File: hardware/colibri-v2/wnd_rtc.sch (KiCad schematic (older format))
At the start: 7 parts

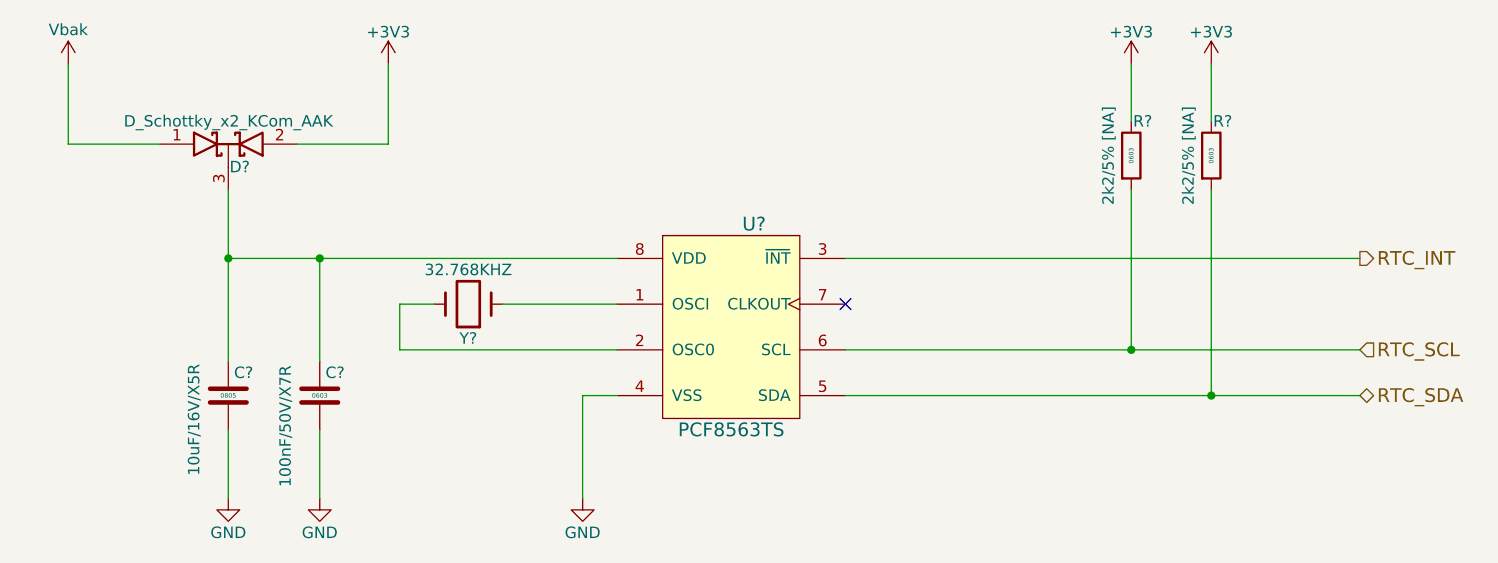
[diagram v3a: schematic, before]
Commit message: Added ext_sensors.sch sheet
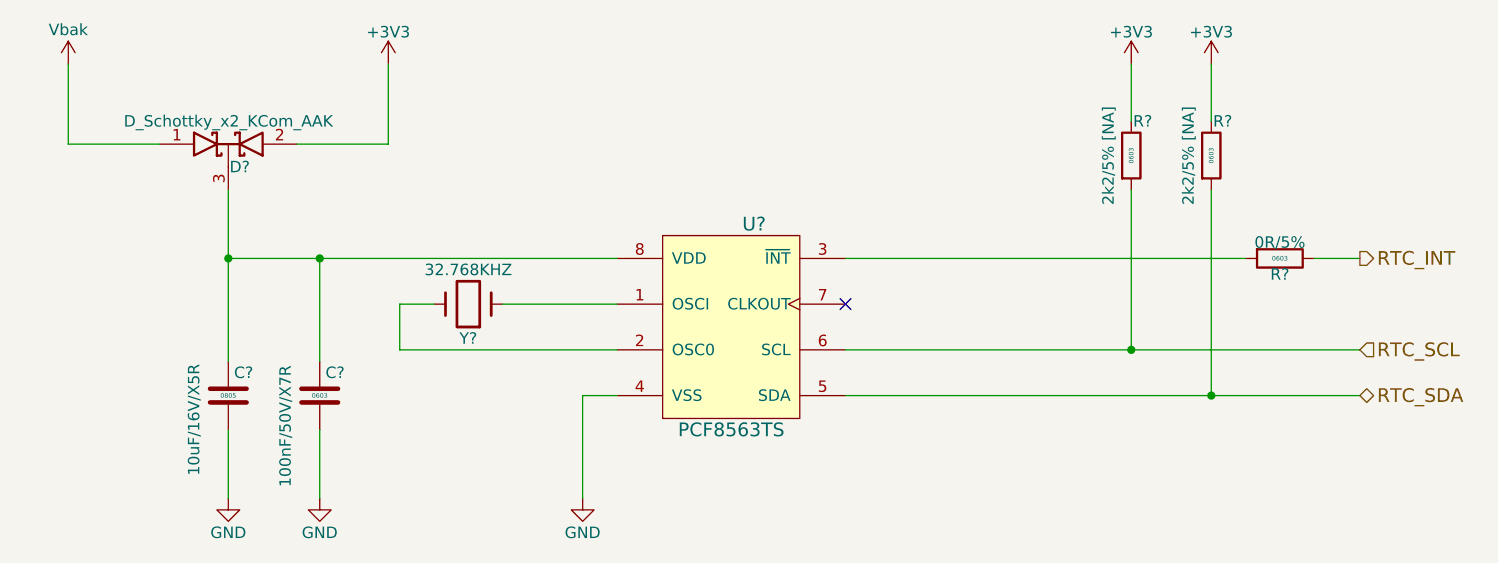
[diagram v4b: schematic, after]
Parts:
- added R?: 0R/5%, Resistors_SMD:R_0603, symbol R_SMT
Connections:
- net RTC_INT: now also R?.1; no longer U?.3 (~INT)
- new net: R?.2, U?.3 (~INT)
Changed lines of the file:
@@
 $Descr A4 11693 8268
 encoding utf-8
-Sheet 19 28
+Sheet 18 28
 Title ""
 Date ""
@@
 NoConn ~ 6000 3300
 Wire Wire Line
-	6000 3100 8250 3100
-Wire Wire Line
 	6000 3500 8250 3500
 Wire Wire Line
@@
 	7600 2800 7600 3700
 Connection ~ 7600 3700
+$Comp
+L R_SMT R?
+U 1 1 56CA065D
+P 7900 3100
+F 0 "R?" V 7970 3100 50  0000 C CNN
+F 1 "0R/5%" V 7830 3100 50  0000 C CNN
+F 2 "Resistors_SMD:R_0603" V 8050 3100 30  0001 C CNN
+F 3 "" V 7980 3100 30  0000 C CNN
+F 4 "0603" V 7900 3100 20  0000 C CNN "SMT"
+F 5 "1469739" V 8100 3100 30  0001 C CNN "Part"
+F 6 "Farnell" V 8150 3100 30  0001 C CNN "Provider"
+	1    7900 3100
+	0    1    1    0
+$EndComp
+Wire Wire Line
+	6000 3100 7750 3100
+Wire Wire Line
+	8050 3100 8250 3100
 $EndSCHEMATC

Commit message: Resolving ERC problems
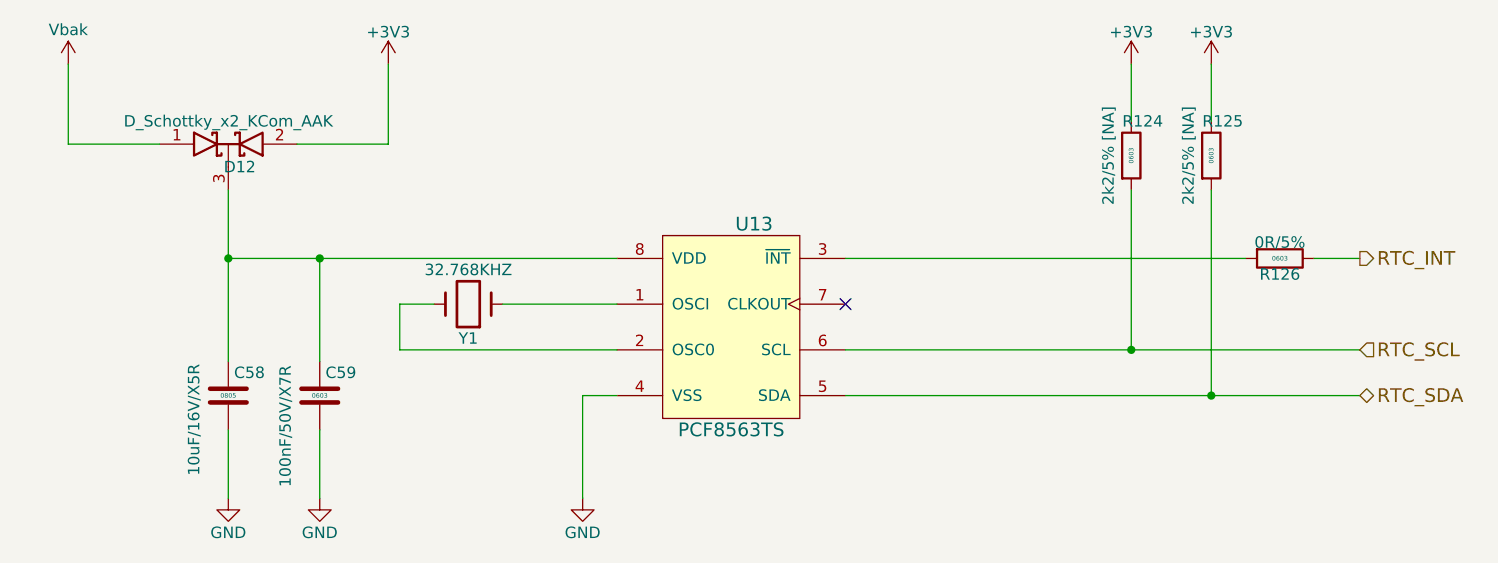
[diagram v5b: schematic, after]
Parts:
- gave numbers to parts that had none: 8
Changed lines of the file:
@@
 EESchema Schematic File Version 2
+LIBS:colibri-wnd-rescue
 LIBS:power
 LIBS:device
@@
 $EndDescr
 $Comp
-L PCF8563TS U?
+L PCF8563TS U13
 U 1 1 565FD554
 P 5500 3400
-F 0 "U?" H 5600 3850 60  0000 C CNN
+F 0 "U13" H 5600 3850 60  0000 C CNN
 F 1 "PCF8563TS" H 5500 2950 60  0000 C CNN
 F 2 "Housings_SSOP:TSSOP-8_3x3mm_Pitch0.65mm" H 5500 2850 60  0001 C CNN
@@
 $EndComp
 $Comp
-L GND #PWR?
+L GND #PWR0161
 U 1 1 565FD5E2
 P 4850 4150
-F 0 "#PWR?" H 4850 3900 50  0001 C CNN
+F 0 "#PWR0161" H 4850 3900 50  0001 C CNN
 F 1 "GND" H 4850 4000 50  0000 C CNN
 F 2 "" H 4850 4150 50  0000 C CNN
@@
 $EndComp
 $Comp
-L +3V3 #PWR?
+L +3V3 #PWR0162
 U 1 1 565FD5F8
 P 4000 2250
-F 0 "#PWR?" H 4000 2100 50  0001 C CNN
+F 0 "#PWR0162" H 4000 2100 50  0001 C CNN
 F 1 "+3V3" H 4000 2390 50  0000 C CNN
 F 2 "" H 4000 2250 50  0000 C CNN
@@
 $EndComp
 $Comp
-L Crystal Y?
+L Crystal Y1
 U 1 1 565FE8B8
 P 4350 3300
-F 0 "Y?" H 4350 3450 50  0000 C CNN
+F 0 "Y1" H 4350 3450 50  0000 C CNN
 F 1 "32.768KHZ" H 4350 3150 50  0000 C CNN
 F 2 "" H 4350 3300 60  0001 C CNN
@@
 	4850 3700 4850 4150
 $Comp
-L D_Schottky_x2_KCom_AAK D?
+L D_Schottky_x2_KCom_AAK D12
 U 1 1 565FE933
 P 3300 2600
-F 0 "D?" H 3350 2500 50  0000 C CNN
+F 0 "D12" H 3350 2500 50  0000 C CNN
 F 1 "D_Schottky_x2_KCom_AAK" H 3300 2700 50  0000 C CNN
 F 2 "" H 3300 2600 50  0000 C CNN
@@
 	2600 2600 3000 2600
 $Comp
-L C_SMT C?
+L C_SMT C59
 U 1 1 56601B22
 P 3700 3700
-F 0 "C?" H 3725 3800 50  0000 L CNN
+F 0 "C59" H 3725 3800 50  0000 L CNN
 F 1 "100nF/50V/X7R" V 3550 3300 50  0000 L CNN
 F 2 "Capacitors_SMD:C_0603" H 3730 3550 30  0001 L CNN
@@
 $EndComp
 $Comp
-L C_SMT C?
+L C_SMT C58
 U 1 1 56601B2C
 P 3300 3700
-F 0 "C?" H 3325 3800 50  0000 L CNN
+F 0 "C58" H 3325 3800 50  0000 L CNN
 F 1 "10uF/16V/X5R" V 3150 3350 50  0000 L CNN
 F 2 "Capacitors_SMD:C_0603" H 3330 3550 30  0001 L CNN
@@
 $EndComp
 $Comp
-L GND #PWR?
+L GND #PWR0163
 U 1 1 56601B52
 P 3700 4150
-F 0 "#PWR?" H 3700 3900 50  0001 C CNN
+F 0 "#PWR0163" H 3700 3900 50  0001 C CNN
 F 1 "GND" H 3700 4000 50  0000 C CNN
 F 2 "" H 3700 4150 50  0000 C CNN
@@
 $EndComp
 $Comp
-L GND #PWR?
+L GND #PWR0164
 U 1 1 56601B71
 P 3300 4150
-F 0 "#PWR?" H 3300 3900 50  0001 C CNN
+F 0 "#PWR0164" H 3300 3900 50  0001 C CNN
 F 1 "GND" H 3300 4000 50  0000 C CNN
 F 2 "" H 3300 4150 50  0000 C CNN
@@
 Connection ~ 3300 3100
 $Comp
-L Vbak #PWR?
+L Vbak #PWR0165
 U 1 1 56602BA4
 P 2600 2250
-F 0 "#PWR?" H 2600 2100 50  0001 C CNN
+F 0 "#PWR0165" H 2600 2100 50  0001 C CNN
 F 1 "Vbak" H 2600 2400 50  0000 C CNN
 F 2 "" H 2600 2250 50  0000 C CNN
@@
 	6000 3700 8250 3700
 $Comp
-L +3V3 #PWR?
+L +3V3 #PWR0166
 U 1 1 56603479
 P 7250 2250
-F 0 "#PWR?" H 7250 2100 50  0001 C CNN
+F 0 "#PWR0166" H 7250 2100 50  0001 C CNN
 F 1 "+3V3" H 7250 2390 50  0000 C CNN
 F 2 "" H 7250 2250 50  0000 C CNN
@@
 $EndComp
 $Comp
-L +3V3 #PWR?
+L +3V3 #PWR0167
 U 1 1 566034CA
 P 7600 2250
-F 0 "#PWR?" H 7600 2100 50  0001 C CNN
+F 0 "#PWR0167" H 7600 2100 50  0001 C CNN
 F 1 "+3V3" H 7600 2390 50  0000 C CNN
 F 2 "" H 7600 2250 50  0000 C CNN
@@
 $EndComp
 $Comp
-L R_SMT R?
+L R_SMT R125
 U 1 1 56606072
 P 7600 2650
-F 0 "R?" H 7650 2800 50  0000 C CNN
+F 0 "R125" H 7650 2800 50  0000 C CNN
 F 1 "2k2/5% [NA]" V 7500 2650 50  0000 C CNN
 F 2 "Resistors_SMD:R_0603" V 7750 2650 30  0001 C CNN
@@
 $EndComp
 $Comp
-L R_SMT R?
+L R_SMT R124
 U 1 1 5660607C
 P 7250 2650
-F 0 "R?" H 7300 2800 50  0000 C CNN
+F 0 "R124" H 7300 2800 50  0000 C CNN
 F 1 "2k2/5% [NA]" V 7150 2650 50  0000 C CNN
 F 2 "Resistors_SMD:R_0603" V 7400 2650 30  0001 C CNN
@@
 Connection ~ 7600 3700
 $Comp
-L R_SMT R?
+L R_SMT R126
 U 1 1 56CA065D
 P 7900 3100
-F 0 "R?" V 7970 3100 50  0000 C CNN
+F 0 "R126" V 7970 3100 50  0000 C CNN
 F 1 "0R/5%" V 7830 3100 50  0000 C CNN
 F 2 "Resistors_SMD:R_0603" V 8050 3100 30  0001 C CNN

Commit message: Fixed ERC errors
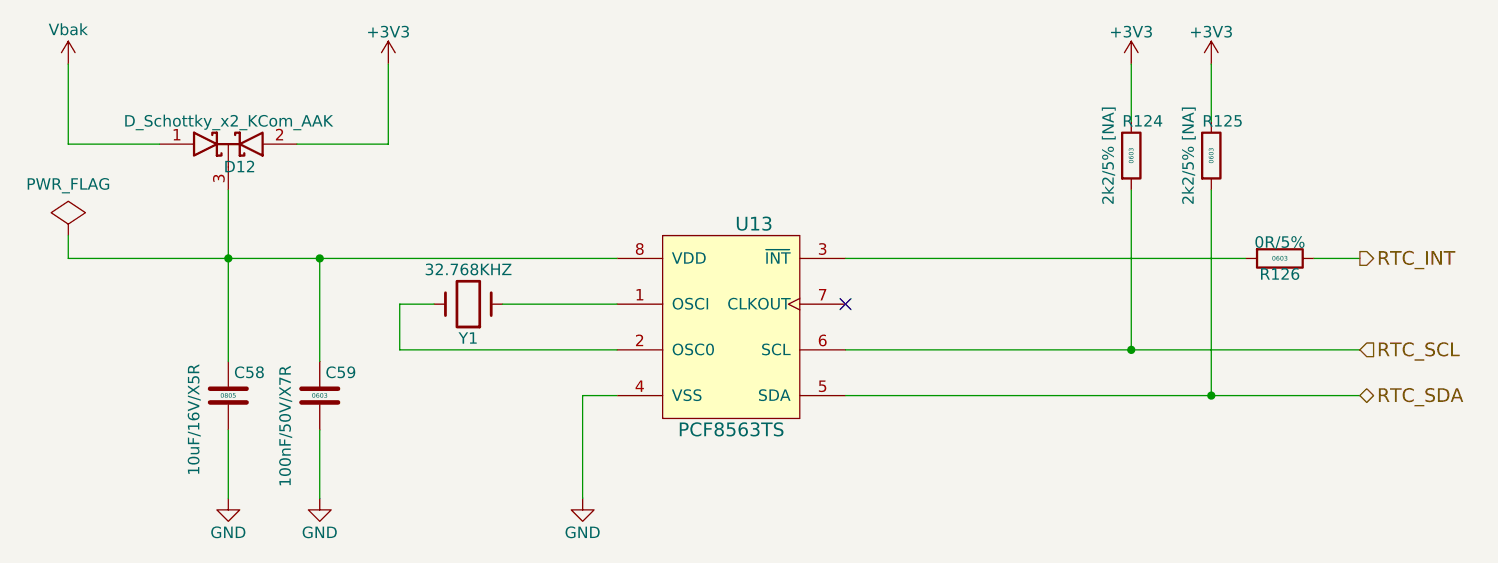
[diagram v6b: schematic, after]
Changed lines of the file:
@@
 $EndComp
 $Comp
-L GND #PWR0161
+L GND #PWR0164
 U 1 1 565FD5E2
 P 4850 4150
-F 0 "#PWR0161" H 4850 3900 50  0001 C CNN
+F 0 "#PWR0164" H 4850 3900 50  0001 C CNN
 F 1 "GND" H 4850 4000 50  0000 C CNN
 F 2 "" H 4850 4150 50  0000 C CNN
@@
 $EndComp
 $Comp
-L +3V3 #PWR0162
+L +3V3 #PWR0165
 U 1 1 565FD5F8
 P 4000 2250
-F 0 "#PWR0162" H 4000 2100 50  0001 C CNN
+F 0 "#PWR0165" H 4000 2100 50  0001 C CNN
 F 1 "+3V3" H 4000 2390 50  0000 C CNN
 F 2 "" H 4000 2250 50  0000 C CNN
@@
 $EndComp
 Wire Wire Line
-	3300 3100 5000 3100
+	2600 3100 5000 3100
 Wire Wire Line
 	3600 2600 4000 2600
@@
 $EndComp
 $Comp
-L GND #PWR0163
+L GND #PWR0166
 U 1 1 56601B52
 P 3700 4150
-F 0 "#PWR0163" H 3700 3900 50  0001 C CNN
+F 0 "#PWR0166" H 3700 3900 50  0001 C CNN
 F 1 "GND" H 3700 4000 50  0000 C CNN
 F 2 "" H 3700 4150 50  0000 C CNN
@@
 $EndComp
 $Comp
-L GND #PWR0164
+L GND #PWR0167
 U 1 1 56601B71
 P 3300 4150
-F 0 "#PWR0164" H 3300 3900 50  0001 C CNN
+F 0 "#PWR0167" H 3300 3900 50  0001 C CNN
 F 1 "GND" H 3300 4000 50  0000 C CNN
 F 2 "" H 3300 4150 50  0000 C CNN
@@
 Connection ~ 3300 3100
 $Comp
-L Vbak #PWR0165
+L Vbak #PWR0168
 U 1 1 56602BA4
 P 2600 2250
-F 0 "#PWR0165" H 2600 2100 50  0001 C CNN
+F 0 "#PWR0168" H 2600 2100 50  0001 C CNN
 F 1 "Vbak" H 2600 2400 50  0000 C CNN
 F 2 "" H 2600 2250 50  0000 C CNN
@@
 	6000 3700 8250 3700
 $Comp
-L +3V3 #PWR0166
+L +3V3 #PWR0169
 U 1 1 56603479
 P 7250 2250
-F 0 "#PWR0166" H 7250 2100 50  0001 C CNN
+F 0 "#PWR0169" H 7250 2100 50  0001 C CNN
 F 1 "+3V3" H 7250 2390 50  0000 C CNN
 F 2 "" H 7250 2250 50  0000 C CNN
@@
 $EndComp
 $Comp
-L +3V3 #PWR0167
+L +3V3 #PWR0170
 U 1 1 566034CA
 P 7600 2250
-F 0 "#PWR0167" H 7600 2100 50  0001 C CNN
+F 0 "#PWR0170" H 7600 2100 50  0001 C CNN
 F 1 "+3V3" H 7600 2390 50  0000 C CNN
 F 2 "" H 7600 2250 50  0000 C CNN
@@
 Wire Wire Line
 	8050 3100 8250 3100
+$Comp
+L PWR_FLAG #FLG0171
+U 1 1 56CC2ED5
+P 2600 3000
+F 0 "#FLG0171" H 2600 3095 50  0001 C CNN
+F 1 "PWR_FLAG" H 2600 3224 50  0000 C CNN
+F 2 "" H 2600 3000 50  0000 C CNN
+F 3 "" H 2600 3000 50  0000 C CNN
+	1    2600 3000
+	1    0    0    -1
+$EndComp
+Wire Wire Line
+	2600 3000 2600 3100
 $EndSCHEMATC
